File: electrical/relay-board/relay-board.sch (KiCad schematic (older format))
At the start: 18 parts, among them P1 CONN_01X03, P2 12V, P3 work, P4 work, P5 probe, P6 probe, P7 output, P8 output gnd, Q1 bc847, Q2 bc847, U1 SPARTAN-SIP-9007, U2 SPARTAN-SIP-9007

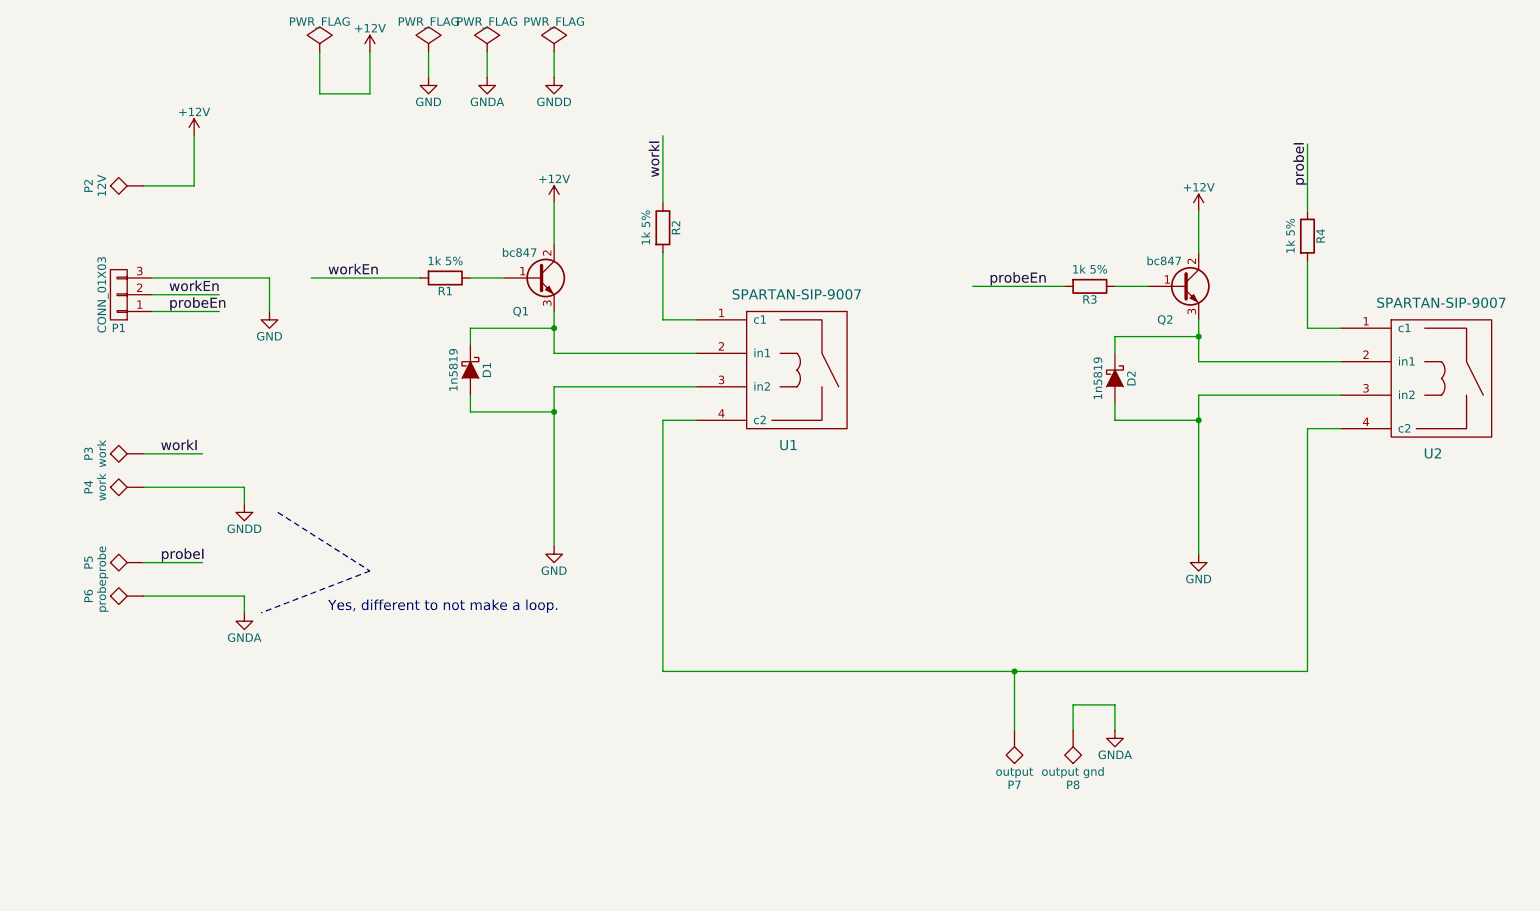
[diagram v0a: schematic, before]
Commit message: Fixed bootloader and verified firmware upgrade routine.
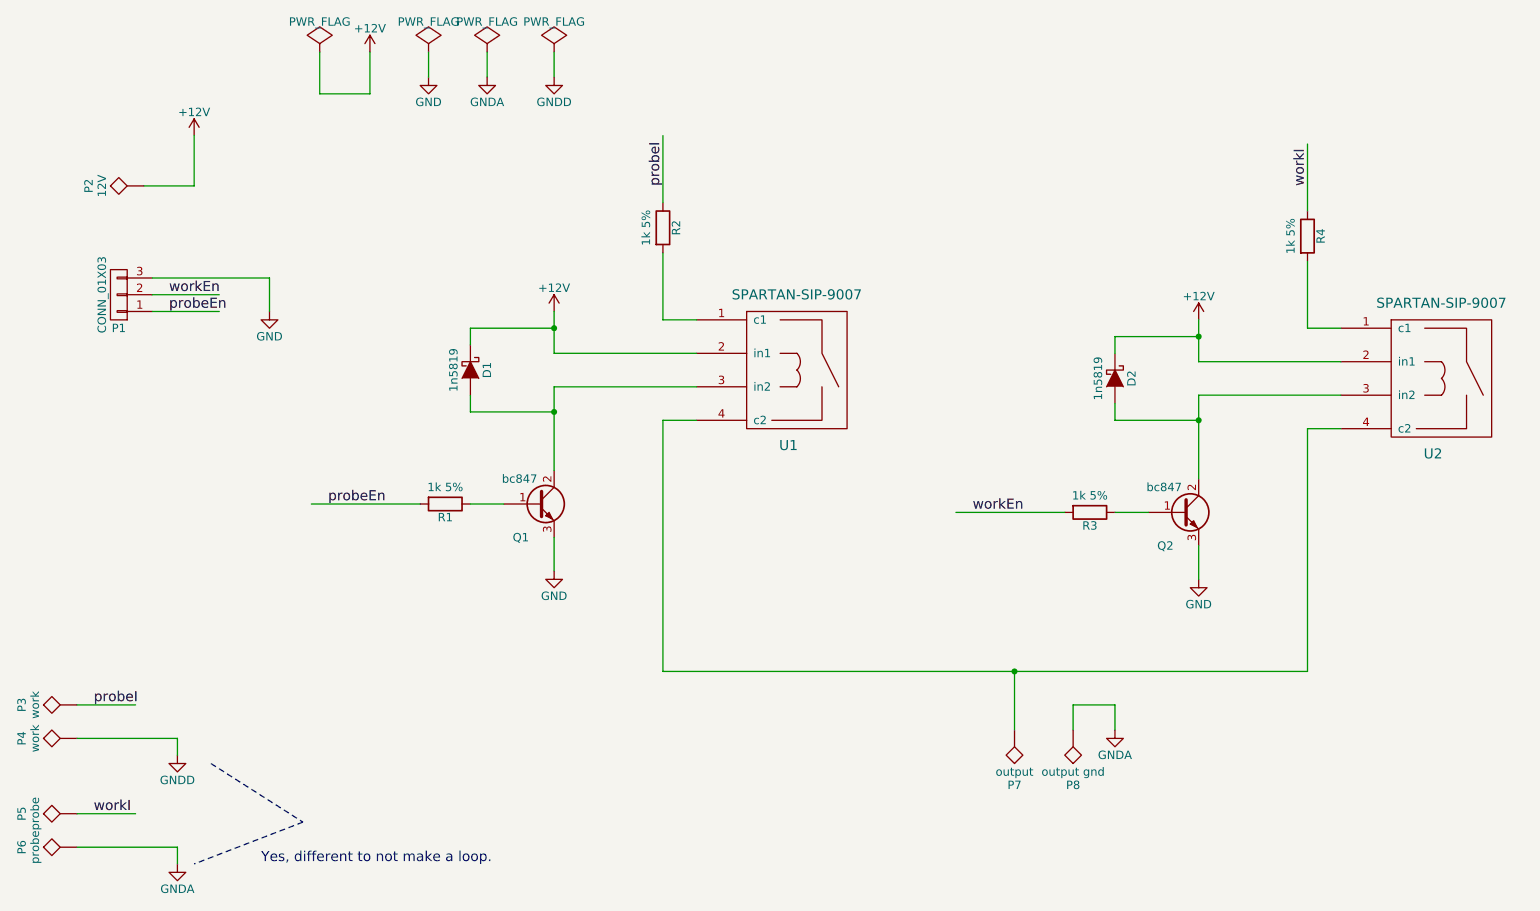
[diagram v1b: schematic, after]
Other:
- moved on the sheet: P3, P4, P5, P6, Q1, R1
